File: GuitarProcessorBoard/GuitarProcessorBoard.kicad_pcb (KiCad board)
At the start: 4 copper layers, 86.2 x 73 mm, 141 parts, among them J1 SWD Header, J2 IO, J3 ScopeGroundLoop, J4 MODE, J5 BYP, SW1 RST, SW3 SW_1, SW4 SW_2, U1 TL074, U2 TL072, U3 TLV320AIC3204, U4 74HC595, U5 STM32H7B0VBT6, U6 AMS1117, U7 TPS63070, Y1 32MHz

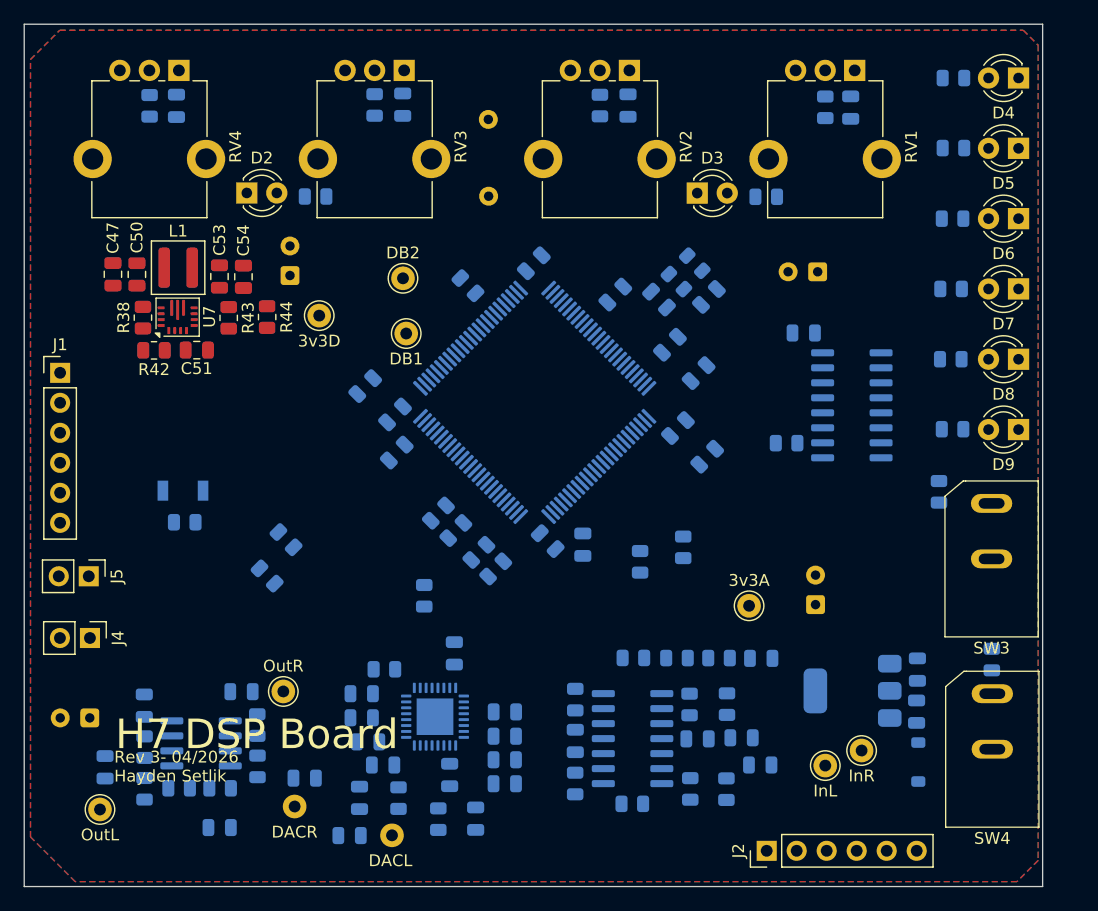
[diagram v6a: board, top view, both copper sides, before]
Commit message: prelim routing, DRC passing
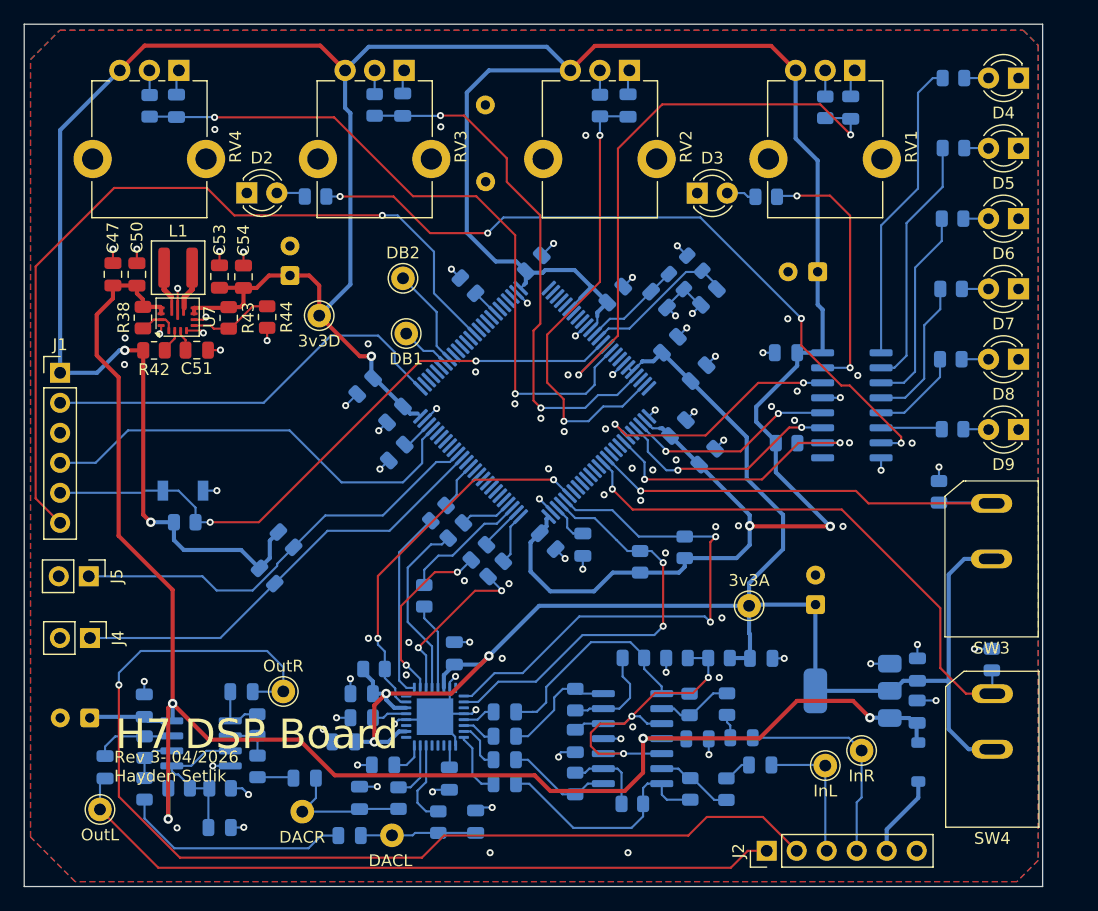
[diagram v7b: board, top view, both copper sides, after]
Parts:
- moved C27 2.24 mm to (-114.6, 58.8)
- moved C17 2.08 mm to (-152.1, 91.7)
- moved J3 1.25 mm to (-140.1, 40.9)
- moved R9 0.88 mm to (-149.5, 85.5)
- moved TP10 0.78 mm to (-155.6, 97.6)
- moved C13 0.31 mm to (-143.1, 94.8)
- moved C16 0.26 mm to (-140.9, 98.5)
- moved R16 0.26 mm to (-144.1, 98.5)
- moved R30 0.12 mm to (-123.2, 75.2)
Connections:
- J2 pad 1: OUT_R -> OUT_L
- J2 pad 2: OUT_L -> OUT_R
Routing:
- net +3.3V: track 0.00 -> 318.2 mm, vias 0 -> 5
- net VCC: track 0.00 -> 143.0 mm, vias 0 -> 4
- net +3.3VA: track 0.00 -> 137.7 mm, vias 0 -> 3
- net GND: track 0.00 -> 98.6 mm, vias 0 -> 100
- net OUT_R: track 0.00 -> 92.5 mm, vias 0 -> 1
- net SWO: track 0.00 -> 69.7 mm, vias 0 -> 1
- net OUT_L: track 0.00 -> 61.9 mm
- net /MCU/LED_TEMPO: track 0.00 -> 61.8 mm, vias 0 -> 4
- net ADC_B: track 0.00 -> 59.0 mm, vias 0 -> 2
- net NRST: track 0.00 -> 54.2 mm, vias 0 -> 2
- net ADC_C: track 0.00 -> 49.8 mm, vias 0 -> 2
- net SWITCH2: track 0.00 -> 46.9 mm, vias 0 -> 1
- net CODEC_SCL: track 0.00 -> 45.3 mm, vias 0 -> 2
- net ADC_D: track 0.00 -> 44.7 mm, vias 0 -> 2
- net ADC_A: track 0.00 -> 38.8 mm, vias 0 -> 2
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
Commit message: stitching vias, silkscreen, spacing
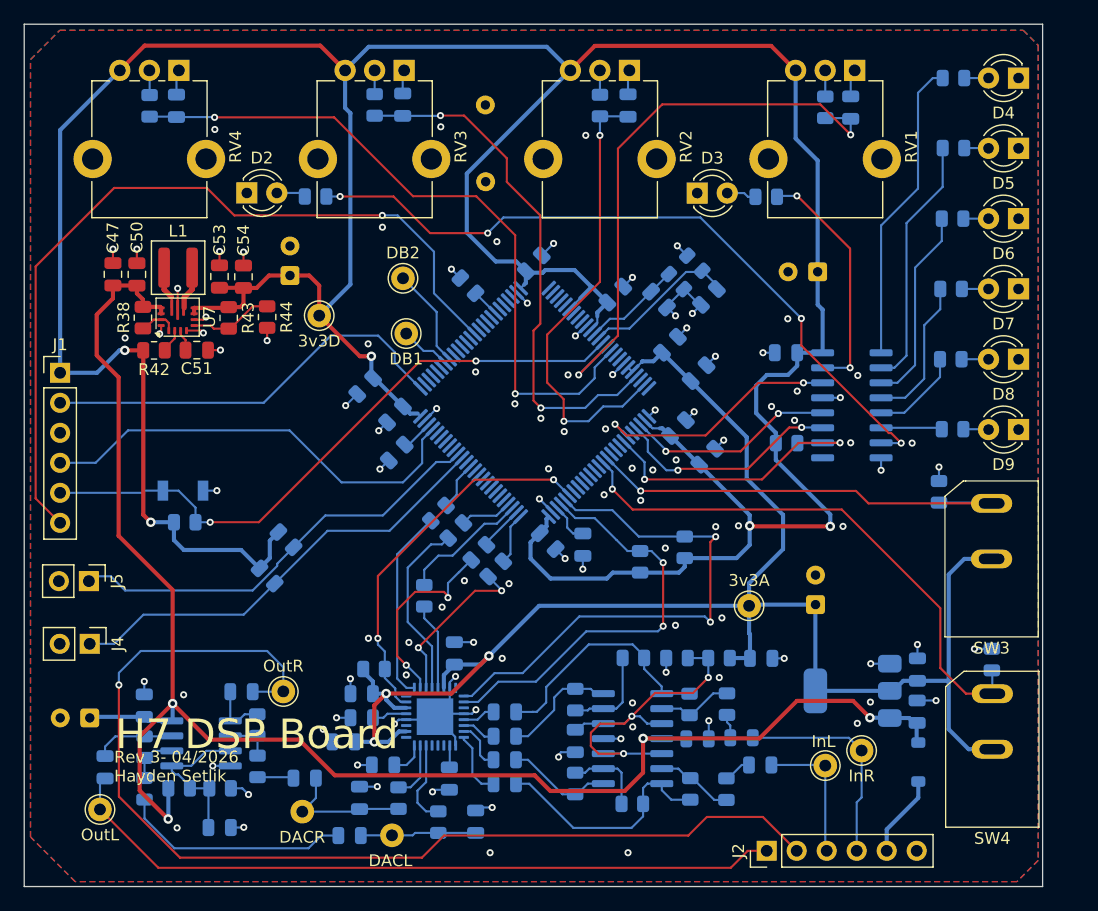
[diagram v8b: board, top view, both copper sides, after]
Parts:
- moved J4 0.50 mm to (-173.6, 83.4)
- moved J5 0.41 mm to (-173.6, 78.1)
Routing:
- net +3.3V: track 318.2 -> 313.7 mm
- net VCC: track 143.0 -> 145.0 mm
- net /MCU/LED_BYPASS: track 22.1 -> 20.5 mm
- net I2S_BCLK: track 15.2 -> 16.7 mm
- net Net-(U1D--): track 8.73 -> 8.05 mm
- net GND: track 98.6 -> 99.1 mm, vias 100 -> 108
- net (no net): vias 1 -> 0
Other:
- board text added: "Alg."
- board text added: "Byp."
